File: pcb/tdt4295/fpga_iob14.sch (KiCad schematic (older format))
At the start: 10 parts

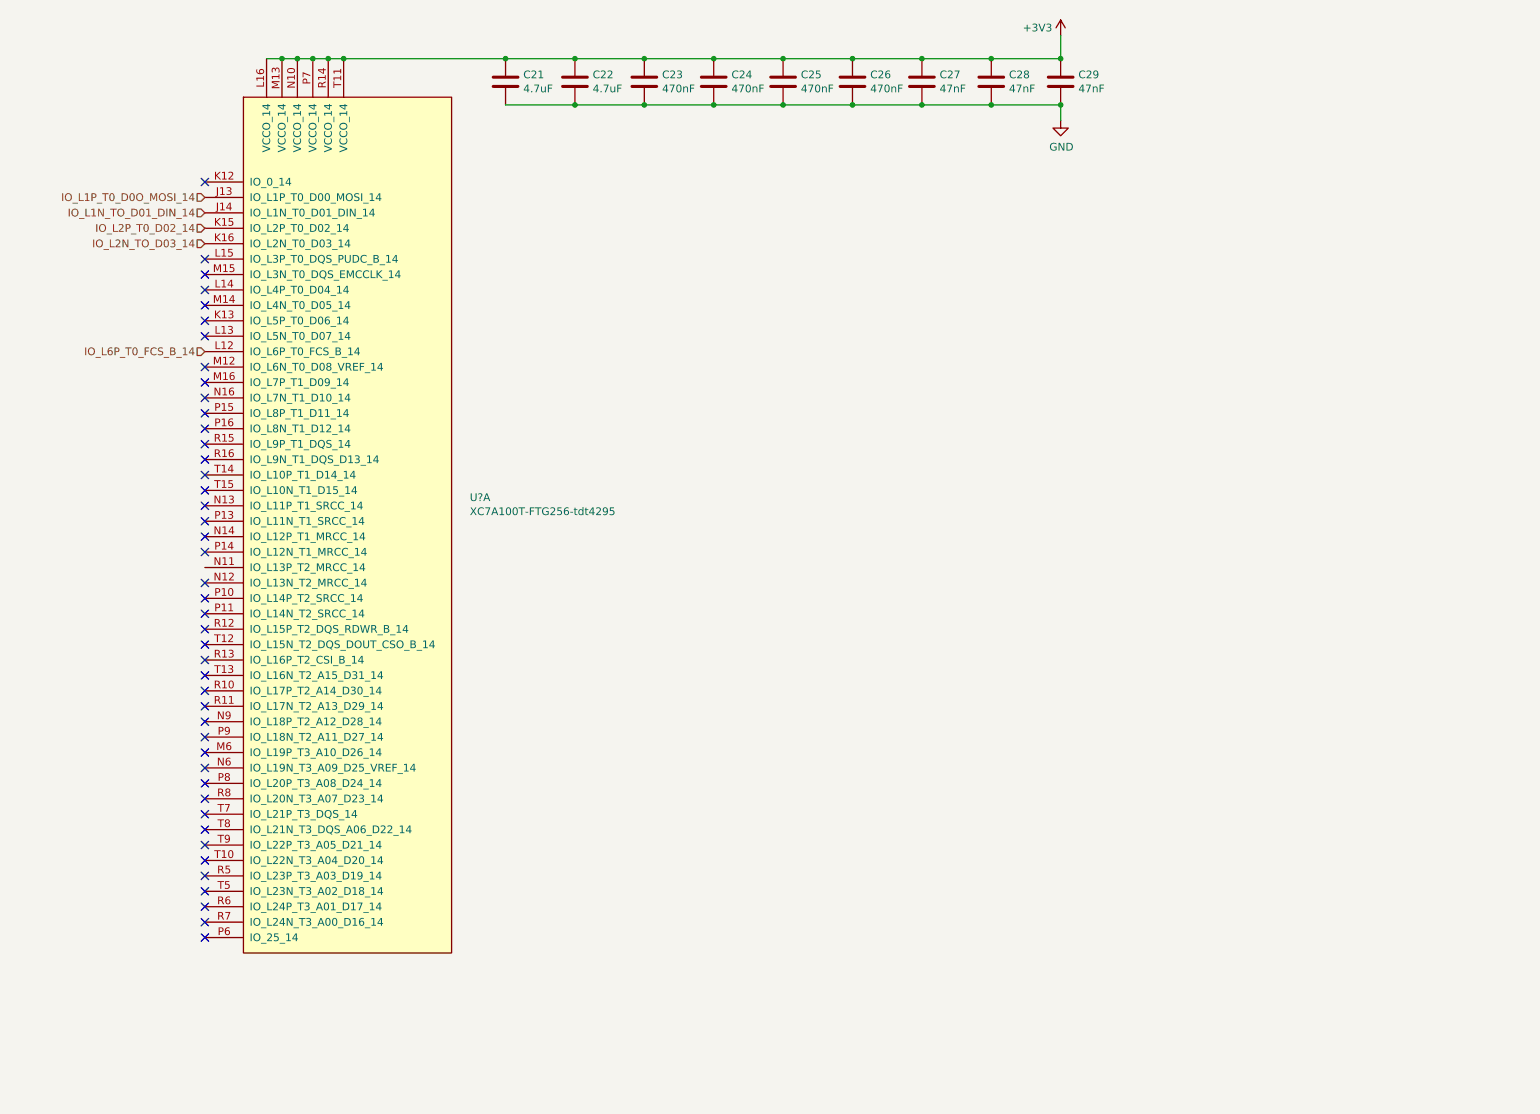
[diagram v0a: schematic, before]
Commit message: fpga external pin headers
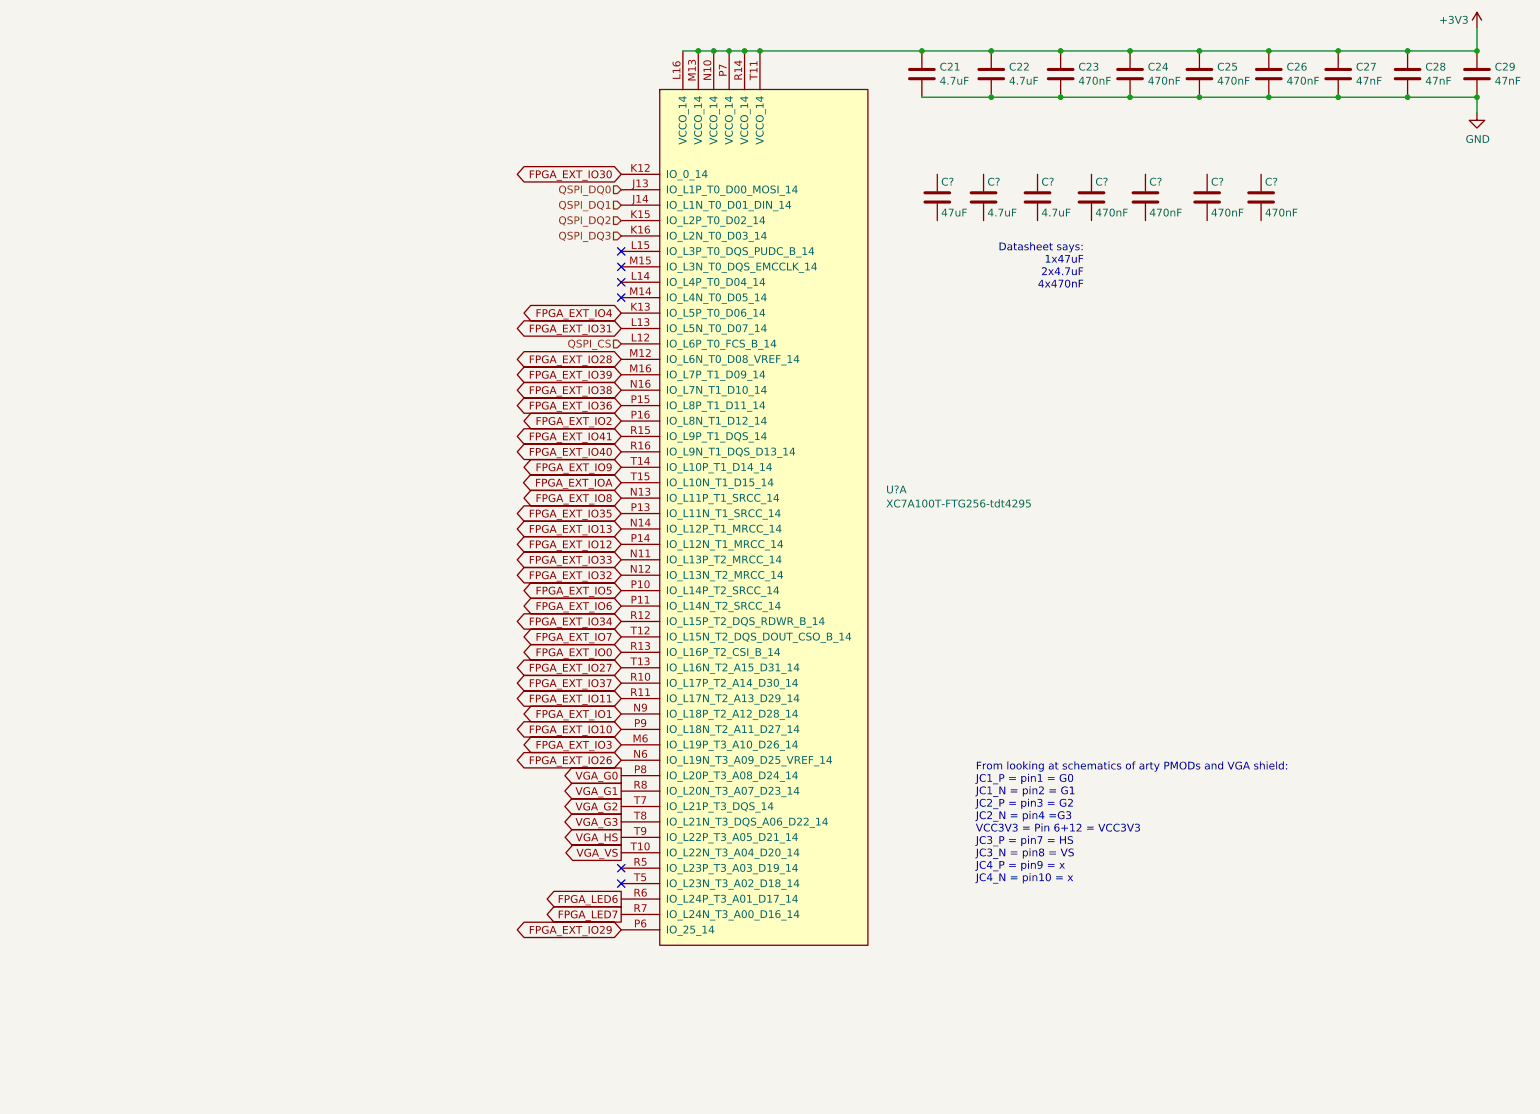
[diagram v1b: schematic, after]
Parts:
- added C?: 47uF, symbol Device:C
- added C? (x2): 4.7uF, symbol Device:C
- added C? (x4): 470nF, symbol Device:C
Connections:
- net FPGA_EXT_IO30: now reaches U?.K12 (IO_0_14)
- net FPGA_EXT_IO4: now reaches U?.K13 (IO_L5P_T0_D06_14)
- net FPGA_EXT_IO31: now reaches U?.L13 (IO_L5N_T0_D07_14)
- net FPGA_EXT_IO28: now reaches U?.M12 (IO_L6N_T0_D08_VREF_14)
- net FPGA_EXT_IO39: now reaches U?.M16 (IO_L7P_T1_D09_14)
- net FPGA_EXT_IO3: now reaches U?.M6 (IO_L19P_T3_A10_D26_14)
- net FPGA_EXT_IO33: now reaches U?.N11 (IO_L13P_T2_MRCC_14)
- net FPGA_EXT_IO32: now reaches U?.N12 (IO_L13N_T2_MRCC_14)
- net FPGA_EXT_IO8: now reaches U?.N13 (IO_L11P_T1_SRCC_14)
- net FPGA_EXT_IO13: now reaches U?.N14 (IO_L12P_T1_MRCC_14)
- net FPGA_EXT_IO38: now reaches U?.N16 (IO_L7N_T1_D10_14)
- net FPGA_EXT_IO26: now reaches U?.N6 (IO_L19N_T3_A09_D25_VREF_14)
- net FPGA_EXT_IO1: now reaches U?.N9 (IO_L18P_T2_A12_D28_14)
- net FPGA_EXT_IO5: now reaches U?.P10 (IO_L14P_T2_SRCC_14)
- net FPGA_EXT_IO6: now reaches U?.P11 (IO_L14N_T2_SRCC_14)
- net FPGA_EXT_IO35: now reaches U?.P13 (IO_L11N_T1_SRCC_14)
- net FPGA_EXT_IO12: now reaches U?.P14 (IO_L12N_T1_MRCC_14)
- net FPGA_EXT_IO36: now reaches U?.P15 (IO_L8P_T1_D11_14)
- net FPGA_EXT_IO2: now reaches U?.P16 (IO_L8N_T1_D12_14)
- net FPGA_EXT_IO29: now reaches U?.P6 (IO_25_14)
- net VGA_G0: now reaches U?.P8 (IO_L20P_T3_A08_D24_14)
- net FPGA_EXT_IO10: now reaches U?.P9 (IO_L18N_T2_A11_D27_14)
- net FPGA_EXT_IO37: now reaches U?.R10 (IO_L17P_T2_A14_D30_14)
- net FPGA_EXT_IO11: now reaches U?.R11 (IO_L17N_T2_A13_D29_14)
- net FPGA_EXT_IO34: now reaches U?.R12 (IO_L15P_T2_DQS_RDWR_B_14)
- net FPGA_EXT_IO0: now reaches U?.R13 (IO_L16P_T2_CSI_B_14)
- net FPGA_EXT_IO41: now reaches U?.R15 (IO_L9P_T1_DQS_14)
- net FPGA_EXT_IO40: now reaches U?.R16 (IO_L9N_T1_DQS_D13_14)
- net FPGA_LED6: now reaches U?.R6 (IO_L24P_T3_A01_D17_14)
- net FPGA_LED7: now reaches U?.R7 (IO_L24N_T3_A00_D16_14)
- net VGA_G1: now reaches U?.R8 (IO_L20N_T3_A07_D23_14)
- net VGA_VS: now reaches U?.T10 (IO_L22N_T3_A04_D20_14)
- net FPGA_EXT_IO7: now reaches U?.T12 (IO_L15N_T2_DQS_DOUT_CSO_B_14)
- net FPGA_EXT_IO27: now reaches U?.T13 (IO_L16N_T2_A15_D31_14)
- net FPGA_EXT_IO9: now reaches U?.T14 (IO_L10P_T1_D14_14)
- net FPGA_EXT_IOA: now reaches U?.T15 (IO_L10N_T1_D15_14)
- net VGA_G2: now reaches U?.T7 (IO_L21P_T3_DQS_14)
- net VGA_G3: now reaches U?.T8 (IO_L21N_T3_DQS_A06_D22_14)
- net VGA_HS: now reaches U?.T9 (IO_L22P_T3_A05_D21_14)
- net IO_L1N_TO_D01_DIN_14 renamed QSPI_DQ1
- net IO_L1P_T0_D0O_MOSI_14 renamed QSPI_DQ0
- net IO_L2N_TO_D03_14 renamed QSPI_DQ3
- net IO_L2P_T0_D02_14 renamed QSPI_DQ2
- net IO_L6P_T0_FCS_B_14 renamed QSPI_CS
- no-connect marks 44 -> 6
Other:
- note added: "Datasheet says:\n1x47uF\n2x4.7uF\n4x470nF"
- note added: "From looking at schematics of arty PMODs and VGA shield:\nJC1_P = pin1 = G0\nJC1_N = pin2 = G1\nJC2_P = pin3 = G2\nJC2_N = pin4 =G3\nVCC3V3 = Pin 6+12 = VCC3V3\nJC3_P = pin7 = HS\nJC3_N = pin8 = VS\nJC4_P = pin9 = x\nJC4_N = pin10 = x"
- moved on the sheet: C21, C22, C23, C24, C25, C26, C27, C28, C29, U?A

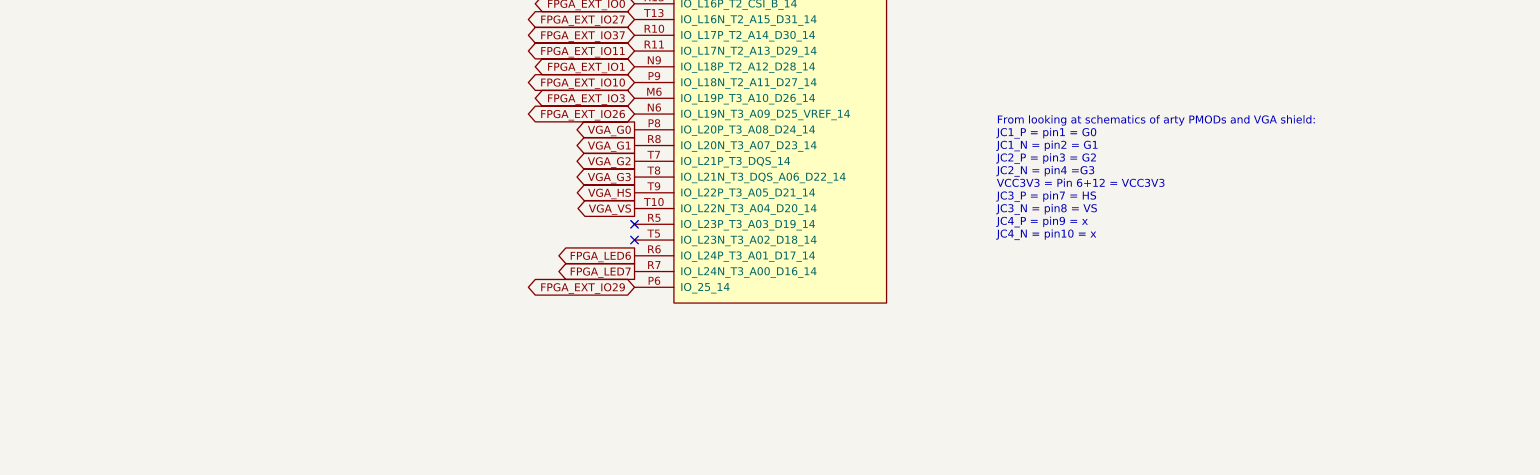
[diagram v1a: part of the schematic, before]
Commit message: Add digikey footprints, implement (some) capacitor footprints in schematic
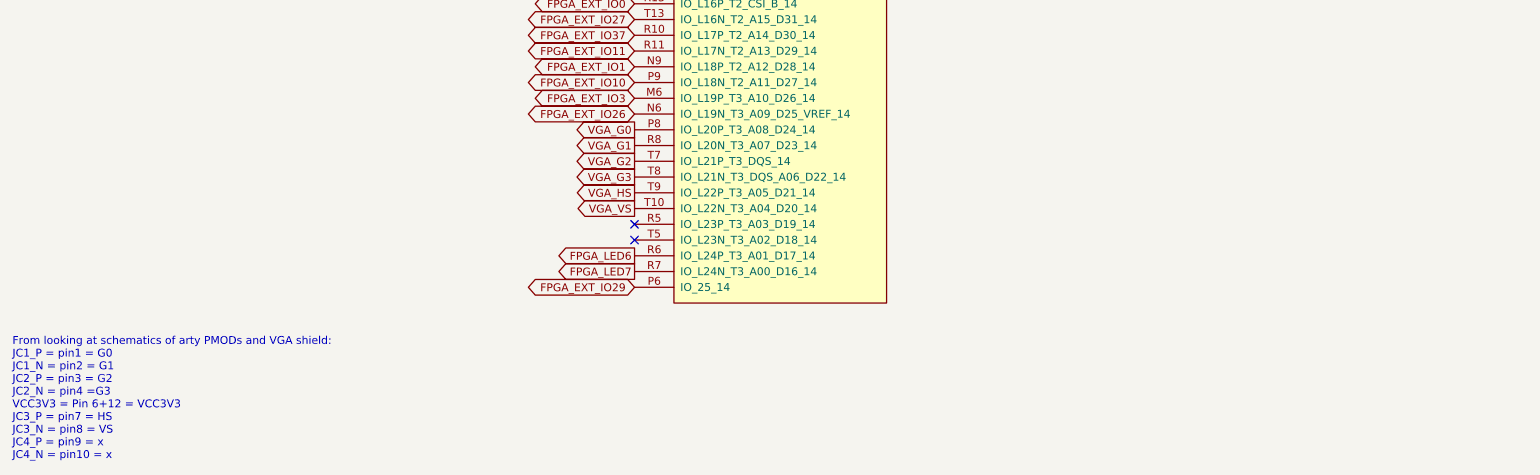
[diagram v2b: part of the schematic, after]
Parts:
- C21, C22, C? (x2): footprint (none) -> Capacitor_SMD:C_0805_2012Metric_Pad1.18x1.45mm_HandSolder
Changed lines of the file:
@@
 F 0 "C21" H 7265 1146 50  0000 L CNN
 F 1 "4.7uF" H 7265 1055 50  0000 L CNN
-F 2 "" H 7188 950 50  0001 C CNN
+F 2 "Capacitor_SMD:C_0805_2012Metric_Pad1.18x1.45mm_HandSolder" H 7188 950 50  0001 C CNN
 F 3 "~" H 7150 1100 50  0001 C CNN
 	1    7150 1100
@@
 F 0 "C22" H 7715 1146 50  0000 L CNN
 F 1 "4.7uF" H 7715 1055 50  0000 L CNN
-F 2 "" H 7638 950 50  0001 C CNN
+F 2 "Capacitor_SMD:C_0805_2012Metric_Pad1.18x1.45mm_HandSolder" H 7638 950 50  0001 C CNN
 F 3 "~" H 7600 1100 50  0001 C CNN
 	1    7600 1100
@@
 Wire Wire Line
 	10300 1250 10750 1250
-Text Notes 7500 6350 0    50   ~ 0
+Text Notes 1250 7750 0    50   ~ 0
 From looking at schematics of arty PMODs and VGA shield:\nJC1_P = pin1 = G0\nJC1_N = pin2 = G1\nJC2_P = pin3 = G2\nJC2_N = pin4 =G3\nVCC3V3 = Pin 6+12 = VCC3V3\nJC3_P = pin7 = HS\nJC3_N = pin8 = VS\nJC4_P = pin9 = x\nJC4_N = pin10 = x
 Text GLabel 5200 5650 0    50   Output ~ 0
@@
 F 0 "C?" H 7575 2000 50  0000 L CNN
 F 1 "4.7uF" H 7575 1800 50  0000 L CNN
-F 2 "" H 7588 1750 50  0001 C CNN
+F 2 "Capacitor_SMD:C_0805_2012Metric_Pad1.18x1.45mm_HandSolder" H 7588 1750 50  0001 C CNN
 F 3 "~" H 7550 1900 50  0001 C CNN
 	1    7550 1900
@@
 F 0 "C?" H 7925 2000 50  0000 L CNN
 F 1 "4.7uF" H 7925 1800 50  0000 L CNN
-F 2 "" H 7938 1750 50  0001 C CNN
+F 2 "Capacitor_SMD:C_0805_2012Metric_Pad1.18x1.45mm_HandSolder" H 7938 1750 50  0001 C CNN
 F 3 "~" H 7900 1900 50  0001 C CNN
 	1    7900 1900

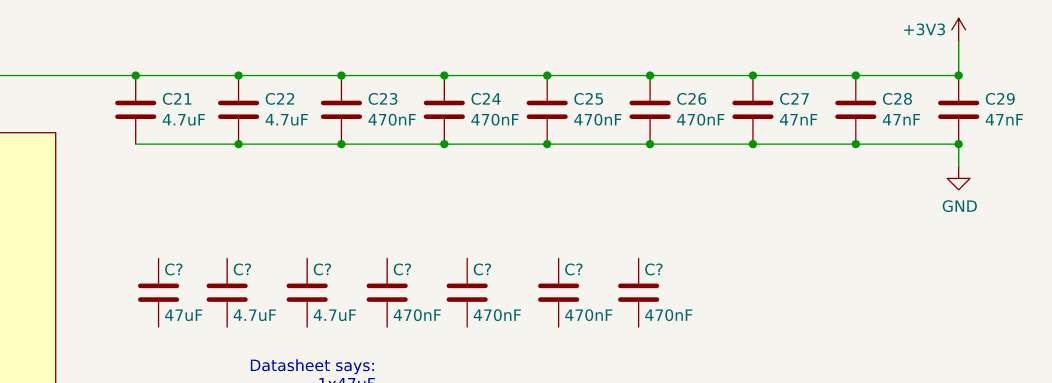
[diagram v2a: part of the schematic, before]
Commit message: connect MCU to FPGA
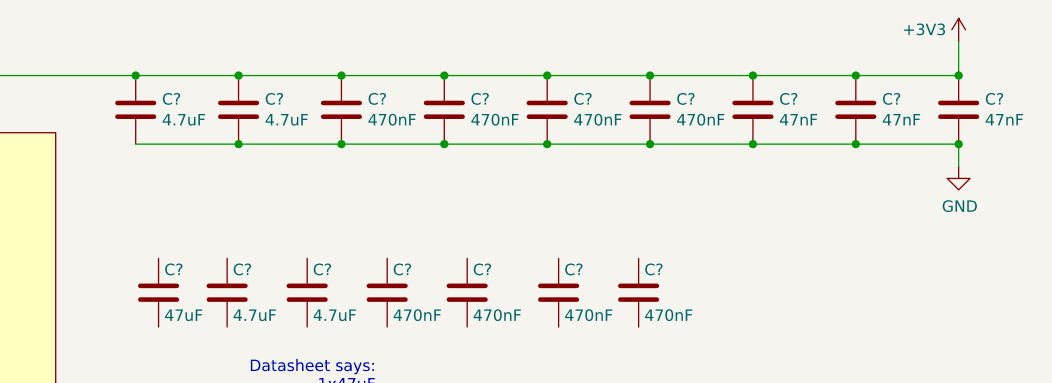
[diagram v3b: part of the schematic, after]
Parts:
- renumbered C21 to C?, C22 to C?, C23 to C?, C24 to C?, C25 to C?, C26 to C?, C27 to C?, C28 to C?, C29 to C?
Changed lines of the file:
@@
 $Descr A4 11693 8268
 encoding utf-8
-Sheet 2 5
+Sheet 4 7
 Title ""
 Date ""
@@
 $EndComp
 $Comp
-L Device:C C21
+L Device:C C?
 U 1 1 614B5319
 P 7150 1100
-F 0 "C21" H 7265 1146 50  0000 L CNN
+F 0 "C?" H 7265 1146 50  0000 L CNN
 F 1 "4.7uF" H 7265 1055 50  0000 L CNN
 F 2 "Capacitor_SMD:C_0805_2012Metric_Pad1.18x1.45mm_HandSolder" H 7188 950 50  0001 C CNN
@@
 	7150 950  7600 950
 $Comp
-L Device:C C22
+L Device:C C?
 U 1 1 614B636F
 P 7600 1100
-F 0 "C22" H 7715 1146 50  0000 L CNN
+F 0 "C?" H 7715 1146 50  0000 L CNN
 F 1 "4.7uF" H 7715 1055 50  0000 L CNN
 F 2 "Capacitor_SMD:C_0805_2012Metric_Pad1.18x1.45mm_HandSolder" H 7638 950 50  0001 C CNN
@@
 	7600 950  8050 950
 $Comp
-L Device:C C23
+L Device:C C?
 U 1 1 614B7D1A
 P 8050 1100
-F 0 "C23" H 8165 1146 50  0000 L CNN
+F 0 "C?" H 8165 1146 50  0000 L CNN
 F 1 "470nF" H 8165 1055 50  0000 L CNN
 F 2 "" H 8088 950 50  0001 C CNN
@@
 Connection ~ 8500 1250
 $Comp
-L Device:C C24
+L Device:C C?
 U 1 1 614B833F
 P 8500 1100
-F 0 "C24" H 8615 1146 50  0000 L CNN
+F 0 "C?" H 8615 1146 50  0000 L CNN
 F 1 "470nF" H 8615 1055 50  0000 L CNN
 F 2 "" H 8538 950 50  0001 C CNN
@@
 $EndComp
 $Comp
-L Device:C C25
+L Device:C C?
 U 1 1 614BA633
 P 8950 1100
-F 0 "C25" H 9065 1146 50  0000 L CNN
+F 0 "C?" H 9065 1146 50  0000 L CNN
 F 1 "470nF" H 9065 1055 50  0000 L CNN
 F 2 "" H 8988 950 50  0001 C CNN
@@
 $EndComp
 $Comp
-L Device:C C26
+L Device:C C?
 U 1 1 614BAE20
 P 9400 1100
-F 0 "C26" H 9515 1146 50  0000 L CNN
+F 0 "C?" H 9515 1146 50  0000 L CNN
 F 1 "470nF" H 9515 1055 50  0000 L CNN
 F 2 "" H 9438 950 50  0001 C CNN
@@
 $EndComp
 $Comp
-L Device:C C27
+L Device:C C?
 U 1 1 614BB1D9
 P 9850 1100
-F 0 "C27" H 9965 1146 50  0000 L CNN
+F 0 "C?" H 9965 1146 50  0000 L CNN
 F 1 "47nF" H 9965 1055 50  0000 L CNN
 F 2 "" H 9888 950 50  0001 C CNN
@@
 $EndComp
 $Comp
-L Device:C C28
+L Device:C C?
 U 1 1 614BB6C0
 P 10300 1100
-F 0 "C28" H 10415 1146 50  0000 L CNN
+F 0 "C?" H 10415 1146 50  0000 L CNN
 F 1 "47nF" H 10415 1055 50  0000 L CNN
 F 2 "" H 10338 950 50  0001 C CNN
@@
 $EndComp
 $Comp
-L Device:C C29
+L Device:C C?
 U 1 1 614BBD0B
 P 10750 1100
-F 0 "C29" H 10865 1146 50  0000 L CNN
+F 0 "C?" H 10865 1146 50  0000 L CNN
 F 1 "47nF" H 10865 1055 50  0000 L CNN
 F 2 "" H 10788 950 50  0001 C CNN
